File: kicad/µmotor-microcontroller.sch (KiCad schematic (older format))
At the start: 20 parts, among them J201 TX, J203 SWDIO, J204 SWCLK, J205 GND

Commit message: layout: components placed
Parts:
- J601: renamed from J205; footprint Measurement_Points:Measurement_Point_Round-SMD-Pad_Small -> Measurement_Point_Round-SMD-Pad_Smaller:Measurement_Point_Round-SMD-Pad_Smaller_0.75mm
- J602: renamed from J204; footprint Measurement_Points:Measurement_Point_Round-SMD-Pad_Small -> Measurement_Point_Round-SMD-Pad_Smaller:Measurement_Point_Round-SMD-Pad_Smaller_0.5mm
- J603: renamed from J203; footprint Measurement_Points:Measurement_Point_Round-SMD-Pad_Small -> Measurement_Point_Round-SMD-Pad_Smaller:Measurement_Point_Round-SMD-Pad_Smaller_0.5mm
- J604: renamed from J201; footprint Measurement_Points:Measurement_Point_Round-SMD-Pad_Small -> Measurement_Point_Round-SMD-Pad_Smaller:Measurement_Point_Round-SMD-Pad_Smaller_0.5mm
- TP601, TP602, TP603: renamed from TP?; footprint (none) -> Measurement_Point_Round-SMD-Pad_Smaller:Measurement_Point_Round-SMD-Pad_Smaller_0.5mm
- U601: renamed from U?; footprint UFQFPN48 -> Housings_DFN_QFN:QFN-48-1EP_7x7mm_Pitch0.5mm
- gave numbers to parts that had none: 3
- renumbered C201 to C601, D201 to D601, R201 to R601
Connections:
- net +3V3: now also U601.1 (VBAT), U601.24 (VDD), U601.36 (VDDUSB), U601.48 (VDD), U601.9 (VDDA/VREF+); no longer U601.1 (VBAT), U601.24 (VDD), U601.36 (VDDUSB), U601.48 (VDD), U601.9 (VDDA/VREF+)
- net BK: now also U601.17 (PA7/ADC1_IN12/COMP2_OUT/I2C3_SCL/LCD_SEG4/QUADSPI_BK1_IO2/SPI1_MOSI/TIM1_CH1N); no longer U601.17 (PA7/ADC1_IN12/COMP2_OUT/I2C3_SCL/LCD_SEG4/QUADSPI_BK1_IO2/SPI1_MOSI/TIM1_CH1N)
- net CAN_RX: now also U601.45 (PB8/CAN1_RX/I2C1_SCL/LCD_SEG16/SAI1_MCLK_A/TIM16_CH1); no longer U601.45 (PB8/CAN1_RX/I2C1_SCL/LCD_SEG16/SAI1_MCLK_A/TIM16_CH1)
- net CAN_TX: now also U601.46 (PB9/CAN1_TX/DAC1_EXTI9/I2C1_SDA/IR_OUT/LCD_COM3/SAI1_FS_A/SPI2_NSS); no longer U601.46 (PB9/CAN1_TX/DAC1_EXTI9/I2C1_SDA/IR_OUT/LCD_COM3/SAI1_FS_A/SPI2_NSS)
- net CS: now also U601.42 (PB6/COMP2_INP/I2C1_SCL/LPTIM1_ETR/SAI1_FS_B/TIM16_CH1N/TSC_G2_IO3/USART1_TX); no longer U601.42 (PB6/COMP2_INP/I2C1_SCL/LPTIM1_ETR/SAI1_FS_B/TIM16_CH1N/TSC_G2_IO3/USART1_TX)
- net DAC: now also U601.15 (PA5/ADC1_IN10/COMP1_INM/COMP2_INM/DAC1_OUT2/LPTIM2_ETR/SPI1_SCK/TIM2_CH1/TIM2_ETR); no longer U601.15 (PA5/ADC1_IN10/COMP1_INM/COMP2_INM/DAC1_OUT2/LPTIM2_ETR/SPI1_SCK/TIM2_CH1/TIM2_ETR)
- net Enc_TIM2_CH1: now also U601.10 (PA0/ADC1_IN5/COMP1_INM/COMP1_OUT/OPAMP1_VINP/RTC_TAMP2/SAI1_EXTCLK/SYS_WKUP1/TIM2_CH1/TIM2_ETR/USART2_CTS); no longer U601.10 (PA0/ADC1_IN5/COMP1_INM/COMP1_OUT/OPAMP1_VINP/RTC_TAMP2/SAI1_EXTCLK/SYS_WKUP1/TIM2_CH1/TIM2_ETR/USART2_CTS)
- net Enc_TIM2_CH2: now also U601.11 (PA1/ADC1_IN6/COMP1_INP/I2C1_SMBA/LCD_SEG0/OPAMP1_VINM/SPI1_SCK/TIM15_CH1N/TIM2_CH2/USART2_DE/USART2_RTS); no longer U601.11 (PA1/ADC1_IN6/COMP1_INP/I2C1_SMBA/LCD_SEG0/OPAMP1_VINM/SPI1_SCK/TIM15_CH1N/TIM2_CH2/USART2_DE/USART2_RTS)
- net GND: now also U601.23 (VSS), U601.35 (VSS), U601.47 (VSS), U601.49 (Pad), U601.8 (VSSA/VREF-); no longer U601.23 (VSS), U601.35 (VSS), U601.47 (VSS), U601.49 (Pad), U601.8 (VSSA/VREF-)
- net GpioB1: now also U601.19 (PB1/ADC1_IN16/COMP1_INM/LCD_SEG6/LPTIM2_IN1/LPUART1_DE/LPUART1_RTS/QUADSPI_BK1_IO0/TIM1_CH3N/USART3_DE/USART3_RTS); no longer U601.19 (PB1/ADC1_IN16/COMP1_INM/LCD_SEG6/LPTIM2_IN1/LPUART1_DE/LPUART1_RTS/QUADSPI_BK1_IO0/TIM1_CH3N/USART3_DE/USART3_RTS)
- net GpioB2: now also U601.20 (PB2/COMP1_INP/I2C3_SMBA/LCD_VLCD/LPTIM1_OUT/RTC_OUT_ALARM/RTC_OUT_CALIB); no longer U601.20 (PB2/COMP1_INP/I2C3_SMBA/LCD_VLCD/LPTIM1_OUT/RTC_OUT_ALARM/RTC_OUT_CALIB)
- net GpioB7: now also U601.43 (PB7/COMP2_INM/I2C1_SDA/LCD_SEG21/LPTIM1_IN2/SYS_PVD_IN/TSC_G2_IO4/USART1_RX); no longer U601.43 (PB7/COMP2_INM/I2C1_SDA/LCD_SEG21/LPTIM1_IN2/SYS_PVD_IN/TSC_G2_IO4/USART1_RX)
- net I2C_SCL: now also U601.21 (PB10/COMP1_OUT/I2C2_SCL/LCD_SEG10/LPUART1_RX/QUADSPI_CLK/SAI1_SCK_A/SPI2_SCK/TIM2_CH3/TSC_SYNC/USART3_TX); no longer U601.21 (PB10/COMP1_OUT/I2C2_SCL/LCD_SEG10/LPUART1_RX/QUADSPI_CLK/SAI1_SCK_A/SPI2_SCK/TIM2_CH3/TSC_SYNC/USART3_TX)
- net I2C_SDA: now also U601.22 (PB11/ADC1_EXTI11/COMP2_OUT/I2C2_SDA/LCD_SEG11/LPUART1_TX/QUADSPI_BK1_NCS/TIM2_CH4/USART3_RX); no longer U601.22 (PB11/ADC1_EXTI11/COMP2_OUT/I2C2_SDA/LCD_SEG11/LPUART1_TX/QUADSPI_BK1_NCS/TIM2_CH4/USART3_RX)
- net LedBlue: now also U601.25 (PB12/I2C2_SMBA/LCD_SEG12/LPUART1_DE/LPUART1_RTS/SAI1_FS_A/SPI2_NSS/SWPMI1_IO/TIM15_BKIN/TIM1_BKIN/TIM1_BKIN_COMP2/TSC_G1_IO1/USART3_CK); no longer U601.3 (PC14-OSC32_IN(PC14)/RCC_OSC32_IN)
- net LedRed: now also U601.5 (PH0-OSC_IN(PH0)/RCC_OSC_IN); no longer U601.2 (PC13/RTC_OUT_ALARM/RTC_OUT_CALIB/RTC_TAMP1/RTC_TS/SYS_WKUP2)
- net MISO: now also U601.40 (PB4(NJTRST)/COMP2_INP/I2C3_SDA/LCD_SEG8/SAI1_MCLK_B/SPI1_MISO/SPI3_MISO/SYS_JTRST/TSC_G2_IO1/USART1_CTS); no longer U601.40 (PB4(NJTRST)/COMP2_INP/I2C3_SDA/LCD_SEG8/SAI1_MCLK_B/SPI1_MISO/SPI3_MISO/SYS_JTRST/TSC_G2_IO1/USART1_CTS)
- net MOSI: now also U601.41 (PB5/COMP2_OUT/I2C1_SMBA/LCD_SEG9/LPTIM1_IN1/SAI1_SD_B/SPI1_MOSI/SPI3_MOSI/TIM16_BKIN/TSC_G2_IO2/USART1_CK); no longer U601.41 (PB5/COMP2_OUT/I2C1_SMBA/LCD_SEG9/LPTIM1_IN1/SAI1_SD_B/SPI1_MOSI/SPI3_MOSI/TIM16_BKIN/TSC_G2_IO2/USART1_CK)
- net PWM_CH1N: now also U601.26 (PB13/I2C2_SCL/LCD_SEG13/LPUART1_CTS/SAI1_SCK_A/SPI2_SCK/SWPMI1_TX/TIM15_CH1N/TIM1_CH1N/TSC_G1_IO2/USART3_CTS); no longer U601.26 (PB13/I2C2_SCL/LCD_SEG13/LPUART1_CTS/SAI1_SCK_A/SPI2_SCK/SWPMI1_TX/TIM15_CH1N/TIM1_CH1N/TSC_G1_IO2/USART3_CTS)
- net PWM_CH1P: now also U601.29 (PA8/LCD_COM0/LPTIM2_OUT/RCC_MCO/SAI1_SCK_A/SWPMI1_IO/TIM1_CH1/USART1_CK); no longer U601.29 (PA8/LCD_COM0/LPTIM2_OUT/RCC_MCO/SAI1_SCK_A/SWPMI1_IO/TIM1_CH1/USART1_CK)
- net PWM_CH2N: now also U601.27 (PB14/I2C2_SDA/LCD_SEG14/SAI1_MCLK_A/SPI2_MISO/SWPMI1_RX/TIM15_CH1/TIM1_CH2N/TSC_G1_IO3/USART3_DE/USART3_RTS); no longer U601.27 (PB14/I2C2_SDA/LCD_SEG14/SAI1_MCLK_A/SPI2_MISO/SWPMI1_RX/TIM15_CH1/TIM1_CH2N/TSC_G1_IO3/USART3_DE/USART3_RTS)
- net PWM_CH2P: now also U601.30 (PA9/DAC1_EXTI9/I2C1_SCL/LCD_COM1/SAI1_FS_A/TIM15_BKIN/TIM1_CH2/USART1_TX); no longer U601.30 (PA9/DAC1_EXTI9/I2C1_SCL/LCD_COM1/SAI1_FS_A/TIM15_BKIN/TIM1_CH2/USART1_TX)
- net PWM_CH3N: now also U601.28 (PB15/ADC1_EXTI15/LCD_SEG15/RTC_REFIN/SAI1_SD_A/SPI2_MOSI/SWPMI1_SUSPEND/TIM15_CH2/TIM1_CH3N/TSC_G1_IO4); no longer U601.28 (PB15/ADC1_EXTI15/LCD_SEG15/RTC_REFIN/SAI1_SD_A/SPI2_MOSI/SWPMI1_SUSPEND/TIM15_CH2/TIM1_CH3N/TSC_G1_IO4)
- net PWM_CH3P: now also U601.31 (PA10/CRS_SYNC/I2C1_SDA/LCD_COM2/SAI1_SD_A/TIM1_CH3/USART1_RX); no longer U601.31 (PA10/CRS_SYNC/I2C1_SDA/LCD_COM2/SAI1_SD_A/TIM1_CH3/USART1_RX)
- net SCK: now also U601.39 (PB3(JTDO-TRACESWO)/COMP2_INM/LCD_SEG7/SAI1_SCK_B/SPI1_SCK/SPI3_SCK/SYS_JTDO-SWO/TIM2_CH2/USART1_DE/USART1_RTS); no longer U601.39 (PB3(JTDO-TRACESWO)/COMP2_INM/LCD_SEG7/SAI1_SCK_B/SPI1_SCK/SPI3_SCK/SYS_JTDO-SWO/TIM2_CH2/USART1_DE/USART1_RTS)
- net SWCLK: now also U601.37 (PA14(JTCK-SWCLK)/I2C1_SMBA/LPTIM1_OUT/SAI1_FS_B/SWPMI1_RX/SYS_JTCK-SWCLK); no longer U601.37 (PA14(JTCK-SWCLK)/I2C1_SMBA/LPTIM1_OUT/SAI1_FS_B/SWPMI1_RX/SYS_JTCK-SWCLK)
- net SWDIO: now also U601.34 (PA13(JTMS-SWDIO)/IR_OUT/SAI1_SD_B/SWPMI1_TX/SYS_JTMS-SWDIO/USB_NOE); no longer U601.34 (PA13(JTMS-SWDIO)/IR_OUT/SAI1_SD_B/SWPMI1_TX/SYS_JTMS-SWDIO/USB_NOE)
- net SenseAll: now also U601.13 (PA3/ADC1_IN8/COMP2_INP/LCD_SEG2/LPUART1_RX/OPAMP1_VOUT/QUADSPI_CLK/SAI1_MCLK_A/TIM15_CH2/TIM2_CH4/USART2_RX), U601.14 (PA4/ADC1_IN9/COMP1_INM/COMP2_INM/DAC1_OUT1/LPTIM2_OUT/SAI1_FS_B/SPI1_NSS/SPI3_NSS/USART2_CK); no longer U601.13 (PA3/ADC1_IN8/COMP2_INP/LCD_SEG2/LPUART1_RX/OPAMP1_VOUT/QUADSPI_CLK/SAI1_MCLK_A/TIM15_CH2/TIM2_CH4/USART2_RX), U601.14 (PA4/ADC1_IN9/COMP1_INM/COMP2_INM/DAC1_OUT1/LPTIM2_OUT/SAI1_FS_B/SPI1_NSS/SPI3_NSS/USART2_CK)
- net SenseV: now also U601.16 (PA6/ADC1_IN11/COMP1_OUT/LCD_SEG3/LPUART1_CTS/QUADSPI_BK1_IO3/SPI1_MISO/TIM16_CH1/TIM1_BKIN/TIM1_BKIN_COMP2/USART3_CTS); no longer U601.16 (PA6/ADC1_IN11/COMP1_OUT/LCD_SEG3/LPUART1_CTS/QUADSPI_BK1_IO3/SPI1_MISO/TIM16_CH1/TIM1_BKIN/TIM1_BKIN_COMP2/USART3_CTS)
- net SenseW: now also U601.18 (PB0/ADC1_IN15/COMP1_OUT/LCD_SEG5/QUADSPI_BK1_IO1/SAI1_EXTCLK/SPI1_NSS/TIM1_CH2N/USART3_CK); no longer U601.18 (PB0/ADC1_IN15/COMP1_OUT/LCD_SEG5/QUADSPI_BK1_IO1/SAI1_EXTCLK/SPI1_NSS/TIM1_CH2N/USART3_CK)
- net TX: now also U601.12 (PA2/ADC1_IN7/COMP2_INM/COMP2_OUT/LCD_SEG1/LPUART1_TX/QUADSPI_BK1_NCS/RCC_LSCO/SYS_WKUP4/TIM15_CH1/TIM2_CH3/USART2_TX); no longer U601.12 (PA2/ADC1_IN7/COMP2_INM/COMP2_OUT/LCD_SEG1/LPUART1_TX/QUADSPI_BK1_NCS/RCC_LSCO/SYS_WKUP4/TIM15_CH1/TIM2_CH3/USART2_TX)
- net ~RST: now also U601.7 (NRST); no longer U601.7 (NRST)
- new net HallU: U601.33 (PA12/CAN1_TX/SPI1_MOSI/TIM1_ETR/USART1_DE/USART1_RTS/USB_DP)
- new net HallV: U601.32 (PA11/ADC1_EXTI11/CAN1_RX/COMP1_OUT/SPI1_MISO/TIM1_BKIN2/TIM1_BKIN2_COMP1/TIM1_CH4/USART1_CTS/USB_DM)
- new net HallW: U601.38 (PA15(JTDI)/ADC1_EXTI15/LCD_SEG17/SPI1_NSS/SPI3_NSS/SWPMI1_SUSPEND/SYS_JTDI/TIM2_CH1/TIM2_ETR/USART2_RX/USART3_DE/USART3_RTS)
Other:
- note added: "Debug LED"
- note removed: "Debug LEDs"
- moved on the sheet: D601, D602, J601, J602, J603, R601, R602

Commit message: layout: routing finished
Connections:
- net CAN_RX: now also U601.32 (PA11/ADC1_EXTI11/CAN1_RX/COMP1_OUT/SPI1_MISO/TIM1_BKIN2/TIM1_BKIN2_COMP1/TIM1_CH4/USART1_CTS/USB_DM); no longer U601.45 (PB8/CAN1_RX/I2C1_SCL/LCD_SEG16/SAI1_MCLK_A/TIM16_CH1)
- net CAN_TX: now also U601.33 (PA12/CAN1_TX/SPI1_MOSI/TIM1_ETR/USART1_DE/USART1_RTS/USB_DP); no longer U601.46 (PB9/CAN1_TX/DAC1_EXTI9/I2C1_SDA/IR_OUT/LCD_COM3/SAI1_FS_A/SPI2_NSS)
- net CS: now also U601.38 (PA15(JTDI)/ADC1_EXTI15/LCD_SEG17/SPI1_NSS/SPI3_NSS/SWPMI1_SUSPEND/SYS_JTDI/TIM2_CH1/TIM2_ETR/USART2_RX/USART3_DE/USART3_RTS); no longer U601.42 (PB6/COMP2_INP/I2C1_SCL/LPTIM1_ETR/SAI1_FS_B/TIM16_CH1N/TSC_G2_IO3/USART1_TX)
- net HallU: now also U601.46 (PB9/CAN1_TX/DAC1_EXTI9/I2C1_SDA/IR_OUT/LCD_COM3/SAI1_FS_A/SPI2_NSS); no longer U601.33 (PA12/CAN1_TX/SPI1_MOSI/TIM1_ETR/USART1_DE/USART1_RTS/USB_DP)
- net HallV: now also U601.45 (PB8/CAN1_RX/I2C1_SCL/LCD_SEG16/SAI1_MCLK_A/TIM16_CH1); no longer U601.32 (PA11/ADC1_EXTI11/CAN1_RX/COMP1_OUT/SPI1_MISO/TIM1_BKIN2/TIM1_BKIN2_COMP1/TIM1_CH4/USART1_CTS/USB_DM)
- net HallW: now also U601.42 (PB6/COMP2_INP/I2C1_SCL/LPTIM1_ETR/SAI1_FS_B/TIM16_CH1N/TSC_G2_IO3/USART1_TX); no longer U601.38 (PA15(JTDI)/ADC1_EXTI15/LCD_SEG17/SPI1_NSS/SPI3_NSS/SWPMI1_SUSPEND/SYS_JTDI/TIM2_CH1/TIM2_ETR/USART2_RX/USART3_DE/USART3_RTS)
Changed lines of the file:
@@
 Text HLabel 3850 3750 0    60   Output ~ 0
 I2C_SCL
-Text HLabel 3850 3950 0    60   Input ~ 0
+Text HLabel 3850 1850 0    60   Input ~ 0
 CAN_RX
-Text HLabel 3850 3850 0    60   Output ~ 0
+Text HLabel 3850 1750 0    60   Output ~ 0
 CAN_TX
 Text HLabel 3850 3450 0    60   Output ~ 0
@@
 	2650 1650 4150 1650
 Wire Wire Line
-	3850 3850 4150 3850
-Wire Wire Line
-	4150 3950 3850 3950
+	3850 1750 4150 1750
+Wire Wire Line
+	4150 1850 3850 1850
 Text HLabel 3850 4450 0    60   Output ~ 0
 SCK
@@
 Text HLabel 3850 4250 0    60   Output ~ 0
 MOSI
-Text HLabel 3850 4150 0    60   Output ~ 0
+Text HLabel 3850 1450 0    60   Output ~ 0
 CS
 Wire Wire Line
@@
 	3850 2350 4150 2350
 Wire Wire Line
-	4150 4150 3850 4150
+	4150 1450 3850 1450
 $Comp
 L R R602
@@
 Wire Wire Line
 	3850 4050 4150 4050
-Text HLabel 3850 1750 0    60   Input ~ 0
+Text HLabel 3850 3850 0    60   Input ~ 0
 HallU
-Text HLabel 3850 1850 0    60   Input ~ 0
+Text HLabel 3850 3950 0    60   Input ~ 0
 HallV
-Text HLabel 3850 1450 0    60   Input ~ 0
+Text HLabel 3850 4150 0    60   Input ~ 0
 HallW
 Wire Wire Line
-	3850 1750 4150 1750
-Wire Wire Line
-	4150 1850 3850 1850
-Wire Wire Line
-	3850 1450 4150 1450
+	3850 3850 4150 3850
+Wire Wire Line
+	4150 3950 3850 3950
+Wire Wire Line
+	3850 4150 4150 4150
 $EndSCHEMATC

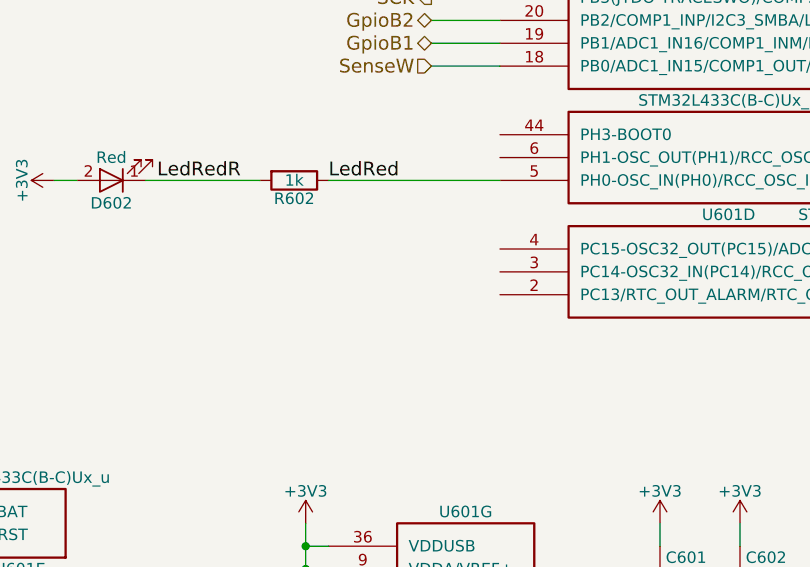
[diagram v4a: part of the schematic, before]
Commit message: layout: minor improvements
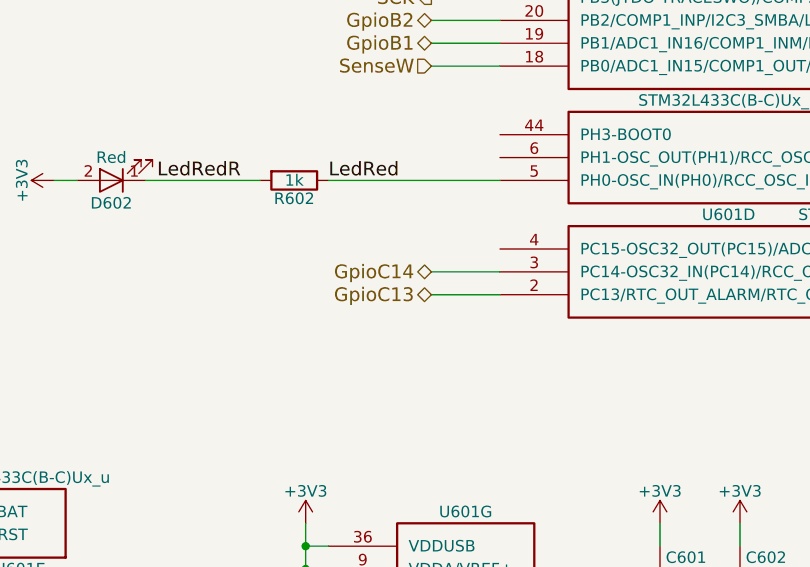
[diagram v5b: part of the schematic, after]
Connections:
- net GpioC13: now reaches U601.2 (PC13/RTC_OUT_ALARM/RTC_OUT_CALIB/RTC_TAMP1/RTC_TS/SYS_WKUP2)
- net GpioC14: now reaches U601.3 (PC14-OSC32_IN(PC14)/RCC_OSC32_IN)
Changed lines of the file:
@@
 $EndComp
 $Comp
-L GND #PWR031
+L GND #PWR034
 U 1 1 59BA1365
 P 2750 1350
-F 0 "#PWR031" H 2750 1100 50  0001 C CNN
+F 0 "#PWR034" H 2750 1100 50  0001 C CNN
 F 1 "GND" H 2750 1200 50  0000 C CNN
 F 2 "" H 2750 1350 50  0001 C CNN
@@
 $EndComp
 $Comp
-L +3V3 #PWR032
+L +3V3 #PWR035
 U 1 1 59BAE1E9
 P 4850 6750
-F 0 "#PWR032" H 4850 6600 50  0001 C CNN
+F 0 "#PWR035" H 4850 6600 50  0001 C CNN
 F 1 "+3V3" H 4850 6890 50  0000 C CNN
 F 2 "" H 4850 6750 50  0001 C CNN
@@
 	4850 6750 4850 6850
 $Comp
-L GND #PWR033
+L GND #PWR036
 U 1 1 59BAE239
 P 4850 7250
-F 0 "#PWR033" H 4850 7000 50  0001 C CNN
+F 0 "#PWR036" H 4850 7000 50  0001 C CNN
 F 1 "GND" H 4850 7100 50  0000 C CNN
 F 2 "" H 4850 7250 50  0001 C CNN
@@
 $EndComp
 $Comp
-L +3V3 #PWR034
+L +3V3 #PWR037
 U 1 1 59BB0D1C
 P 1500 3550
-F 0 "#PWR034" H 1500 3400 50  0001 C CNN
+F 0 "#PWR037" H 1500 3400 50  0001 C CNN
 F 1 "+3V3" H 1500 3690 50  0000 C CNN
 F 2 "" H 1500 3550 50  0001 C CNN
@@
 ~RST
 $Comp
-L GND #PWR035
+L GND #PWR038
 U 1 1 5A5173EC
 P 5700 7100
-F 0 "#PWR035" H 5700 6850 50  0001 C CNN
+F 0 "#PWR038" H 5700 6850 50  0001 C CNN
 F 1 "GND" H 5700 6950 50  0000 C CNN
 F 2 "" H 5700 7100 50  0001 C CNN
@@
 Connection ~ 5700 7000
 $Comp
-L +3V3 #PWR036
+L +3V3 #PWR039
 U 1 1 5A517858
 P 3300 6750
-F 0 "#PWR036" H 3300 6600 50  0001 C CNN
+F 0 "#PWR039" H 3300 6600 50  0001 C CNN
 F 1 "+3V3" H 3300 6890 50  0000 C CNN
 F 2 "" H 3300 6750 50  0001 C CNN
@@
 $EndComp
 $Comp
-L +3V3 #PWR037
+L +3V3 #PWR040
 U 1 1 5A5277F8
 P 2200 5250
-F 0 "#PWR037" H 2200 5100 50  0001 C CNN
+F 0 "#PWR040" H 2200 5100 50  0001 C CNN
 F 1 "+3V3" H 2200 5390 50  0000 C CNN
 F 2 "" H 2200 5250 50  0001 C CNN
@@
 $EndComp
 $Comp
-L +3V3 #PWR038
+L +3V3 #PWR041
 U 1 1 5A537A1D
 P 1450 6600
-F 0 "#PWR038" H 1450 6450 50  0001 C CNN
+F 0 "#PWR041" H 1450 6450 50  0001 C CNN
 F 1 "+3V3" H 1450 6740 50  0000 C CNN
 F 2 "" H 1450 6600 50  0001 C CNN
@@
 $EndComp
 $Comp
-L +3V3 #PWR039
+L +3V3 #PWR042
 U 1 1 5A538747
 P 5200 6750
-F 0 "#PWR039" H 5200 6600 50  0001 C CNN
+F 0 "#PWR042" H 5200 6600 50  0001 C CNN
 F 1 "+3V3" H 5200 6890 50  0000 C CNN
 F 2 "" H 5200 6750 50  0001 C CNN
@@
 	5200 6750 5200 6850
 $Comp
-L GND #PWR040
+L GND #PWR043
 U 1 1 5A53874E
 P 5200 7250
-F 0 "#PWR040" H 5200 7000 50  0001 C CNN
+F 0 "#PWR043" H 5200 7000 50  0001 C CNN
 F 1 "GND" H 5200 7100 50  0000 C CNN
 F 2 "" H 5200 7250 50  0001 C CNN
@@
 Wire Wire Line
 	3850 4150 4150 4150
+Text HLabel 3850 5650 0    60   BiDi ~ 0
+GpioC14
+Text HLabel 3850 5750 0    60   BiDi ~ 0
+GpioC13
+Wire Wire Line
+	3850 5650 4150 5650
+Wire Wire Line
+	4150 5750 3850 5750
 $EndSCHEMATC

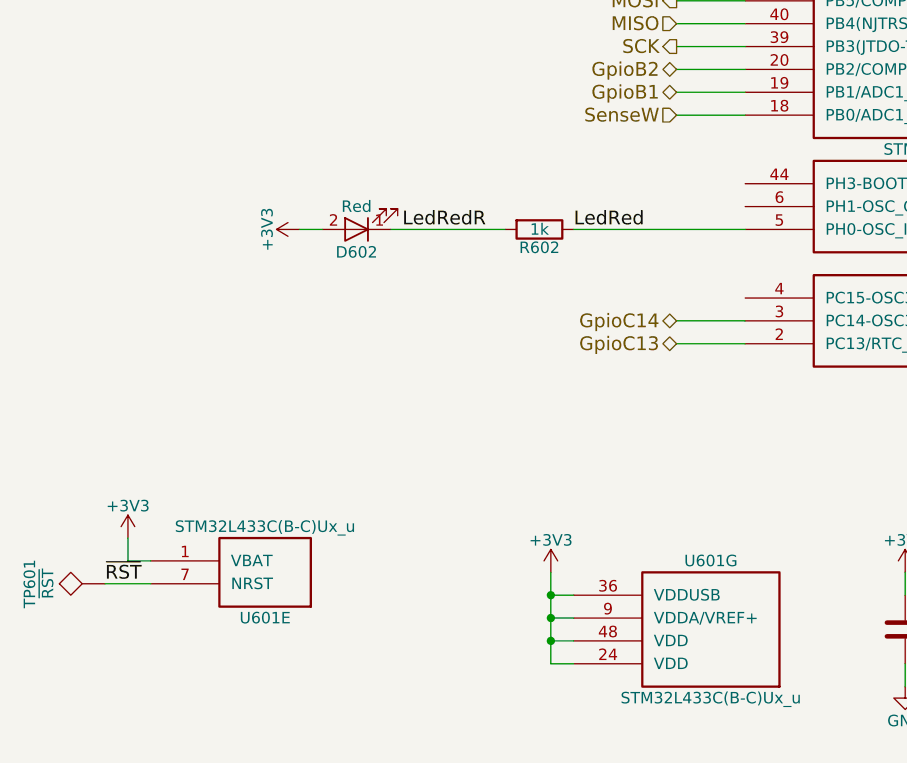
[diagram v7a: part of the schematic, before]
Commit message: layout: improvements
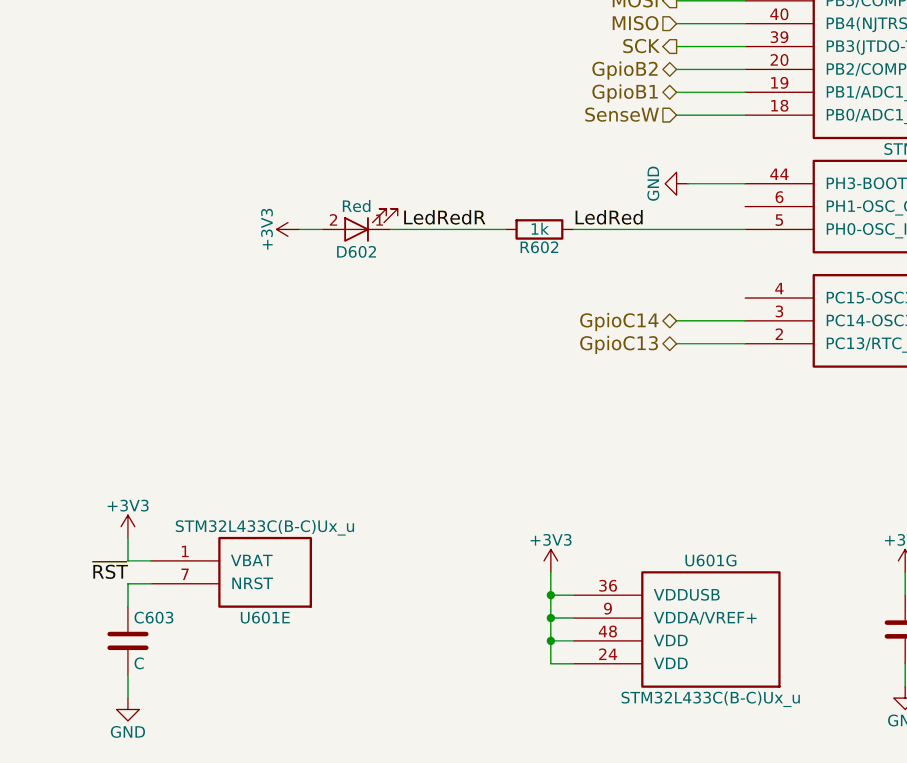
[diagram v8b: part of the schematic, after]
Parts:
- removed TP601: ~RST, Measurement_Point_Round-SMD-Pad_Smaller:Measurement_Point_Round-SMD-Pad_Smaller_0.5mm, symbol TEST
- added C603: C, Capacitors_SMD:C_0402, symbol C
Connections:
- net GND: now also U601.44 (PH3-BOOT0), C603.2
- net ~RST: now also C603.1
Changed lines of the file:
@@
 $EndComp
 $Comp
-L GND #PWR604
+L GND #PWR038
 U 1 1 59BA1365
 P 2750 1350
-F 0 "#PWR604" H 2750 1100 50  0001 C CNN
+F 0 "#PWR038" H 2750 1100 50  0001 C CNN
 F 1 "GND" H 2750 1200 50  0000 C CNN
 F 2 "" H 2750 1350 50  0001 C CNN
@@
 $EndComp
 $Comp
-L +3V3 #PWR606
+L +3V3 #PWR039
 U 1 1 59BAE1E9
 P 4850 6750
-F 0 "#PWR606" H 4850 6600 50  0001 C CNN
+F 0 "#PWR039" H 4850 6600 50  0001 C CNN
 F 1 "+3V3" H 4850 6890 50  0000 C CNN
 F 2 "" H 4850 6750 50  0001 C CNN
@@
 	4850 6750 4850 6850
 $Comp
-L GND #PWR607
+L GND #PWR040
 U 1 1 59BAE239
 P 4850 7250
-F 0 "#PWR607" H 4850 7000 50  0001 C CNN
+F 0 "#PWR040" H 4850 7000 50  0001 C CNN
 F 1 "GND" H 4850 7100 50  0000 C CNN
 F 2 "" H 4850 7250 50  0001 C CNN
@@
 $EndComp
 $Comp
-L +3V3 #PWR602
+L +3V3 #PWR041
 U 1 1 59BB0D1C
 P 1500 3550
-F 0 "#PWR602" H 1500 3400 50  0001 C CNN
+F 0 "#PWR041" H 1500 3400 50  0001 C CNN
 F 1 "+3V3" H 1500 3690 50  0000 C CNN
 F 2 "" H 1500 3550 50  0001 C CNN
@@
 Wire Wire Line
 	1900 3550 2400 3550
-$Comp
-L TEST TP601
-U 1 1 5A516FC4
-P 1350 6800
-F 0 "TP601" H 1350 7100 50  0000 C BNN
-F 1 "~RST" H 1350 7050 50  0000 C CNN
-F 2 "Measurement_Point_Round-SMD-Pad_Smaller:Measurement_Point_Round-SMD-Pad_Smaller_0.5mm" H 1350 6800 50  0001 C CNN
-F 3 "" H 1350 6800 50  0001 C CNN
-	1    1350 6800
-	0    -1   -1   0
-$EndComp
-Wire Wire Line
-	1350 6800 1550 6800
-Text Label 1350 6800 0    60   ~ 0
+Text Label 1450 6800 2    60   ~ 0
 ~RST
 $Comp
-L GND #PWR610
+L GND #PWR042
 U 1 1 5A5173EC
 P 5700 7100
-F 0 "#PWR610" H 5700 6850 50  0001 C CNN
+F 0 "#PWR042" H 5700 6850 50  0001 C CNN
 F 1 "GND" H 5700 6950 50  0000 C CNN
 F 2 "" H 5700 7100 50  0001 C CNN
@@
 Connection ~ 5700 7000
 $Comp
-L +3V3 #PWR605
+L +3V3 #PWR043
 U 1 1 5A517858
 P 3300 6750
-F 0 "#PWR605" H 3300 6600 50  0001 C CNN
+F 0 "#PWR043" H 3300 6600 50  0001 C CNN
 F 1 "+3V3" H 3300 6890 50  0000 C CNN
 F 2 "" H 3300 6750 50  0001 C CNN
@@
 $EndComp
 $Comp
-L +3V3 #PWR603
+L +3V3 #PWR044
 U 1 1 5A5277F8
 P 2200 5250
-F 0 "#PWR603" H 2200 5100 50  0001 C CNN
+F 0 "#PWR044" H 2200 5100 50  0001 C CNN
 F 1 "+3V3" H 2200 5390 50  0000 C CNN
 F 2 "" H 2200 5250 50  0001 C CNN
@@
 $EndComp
 $Comp
-L +3V3 #PWR601
+L +3V3 #PWR045
 U 1 1 5A537A1D
 P 1450 6600
-F 0 "#PWR601" H 1450 6450 50  0001 C CNN
+F 0 "#PWR045" H 1450 6450 50  0001 C CNN
 F 1 "+3V3" H 1450 6740 50  0000 C CNN
 F 2 "" H 1450 6600 50  0001 C CNN
@@
 $EndComp
 $Comp
-L +3V3 #PWR608
+L +3V3 #PWR046
 U 1 1 5A538747
 P 5200 6750
-F 0 "#PWR608" H 5200 6600 50  0001 C CNN
+F 0 "#PWR046" H 5200 6600 50  0001 C CNN
 F 1 "+3V3" H 5200 6890 50  0000 C CNN
 F 2 "" H 5200 6750 50  0001 C CNN
@@
 	5200 6750 5200 6850
 $Comp
-L GND #PWR609
+L GND #PWR047
 U 1 1 5A53874E
 P 5200 7250
-F 0 "#PWR609" H 5200 7000 50  0001 C CNN
+F 0 "#PWR047" H 5200 7000 50  0001 C CNN
 F 1 "GND" H 5200 7100 50  0000 C CNN
 F 2 "" H 5200 7250 50  0001 C CNN
@@
 Wire Wire Line
 	4150 5750 3850 5750
+$Comp
+L C C603
+U 1 1 5A7A4571
+P 1450 7050
+F 0 "C603" H 1475 7150 50  0000 L CNN
+F 1 "C" H 1475 6950 50  0000 L CNN
+F 2 "Capacitors_SMD:C_0402" H 1488 6900 50  0001 C CNN
+F 3 "" H 1450 7050 50  0001 C CNN
+	1    1450 7050
+	1    0    0    -1
+$EndComp
+$Comp
+L GND #PWR048
+U 1 1 5A7A45EE
+P 1450 7300
+F 0 "#PWR048" H 1450 7050 50  0001 C CNN
+F 1 "GND" H 1450 7150 50  0000 C CNN
+F 2 "" H 1450 7300 50  0001 C CNN
+F 3 "" H 1450 7300 50  0001 C CNN
+	1    1450 7300
+	1    0    0    -1
+$EndComp
+Wire Wire Line
+	1450 7300 1450 7200
+Wire Wire Line
+	1550 6800 1450 6800
+Wire Wire Line
+	1450 6800 1450 6900
+$Comp
+L GND #PWR049
+U 1 1 5A7BB389
+P 3900 5050
+F 0 "#PWR049" H 3900 4800 50  0001 C CNN
+F 1 "GND" H 3900 4900 50  0000 C CNN
+F 2 "" H 3900 5050 50  0001 C CNN
+F 3 "" H 3900 5050 50  0001 C CNN
+	1    3900 5050
+	0    1    1    0
+$EndComp
+Wire Wire Line
+	3900 5050 4150 5050
 $EndSCHEMATC
